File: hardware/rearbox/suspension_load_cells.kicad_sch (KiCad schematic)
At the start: 15 parts, among them U31 NAU7802SGI

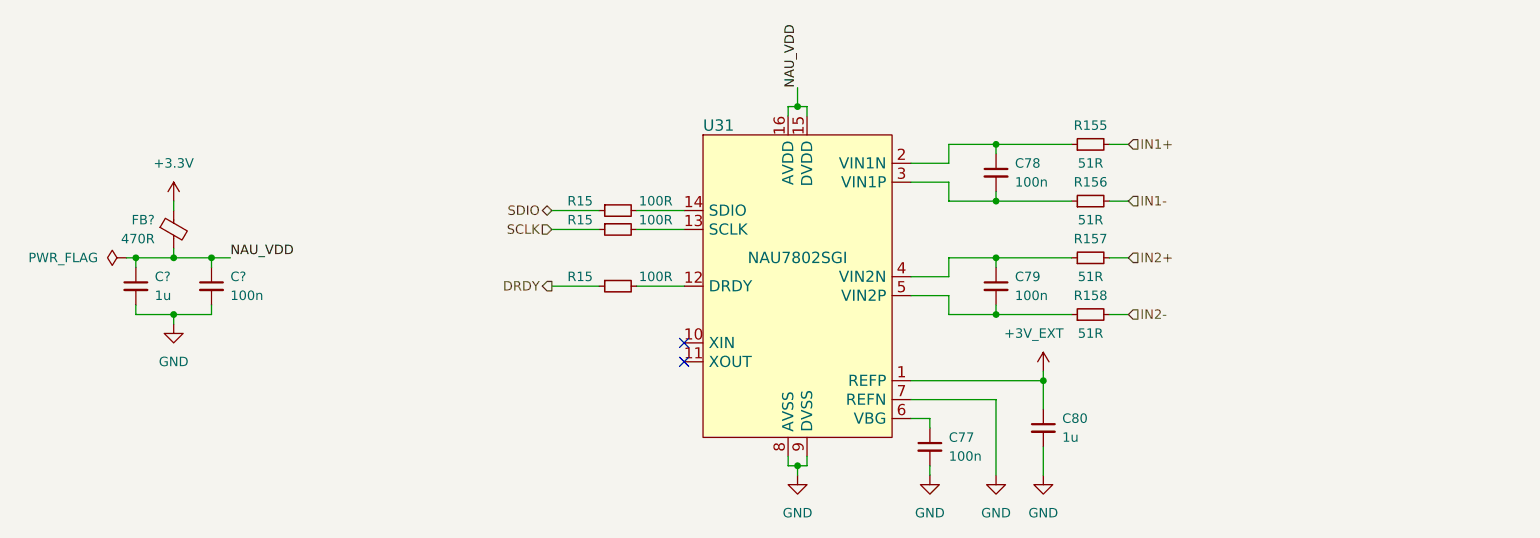
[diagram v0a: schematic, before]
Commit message: Add the connector board
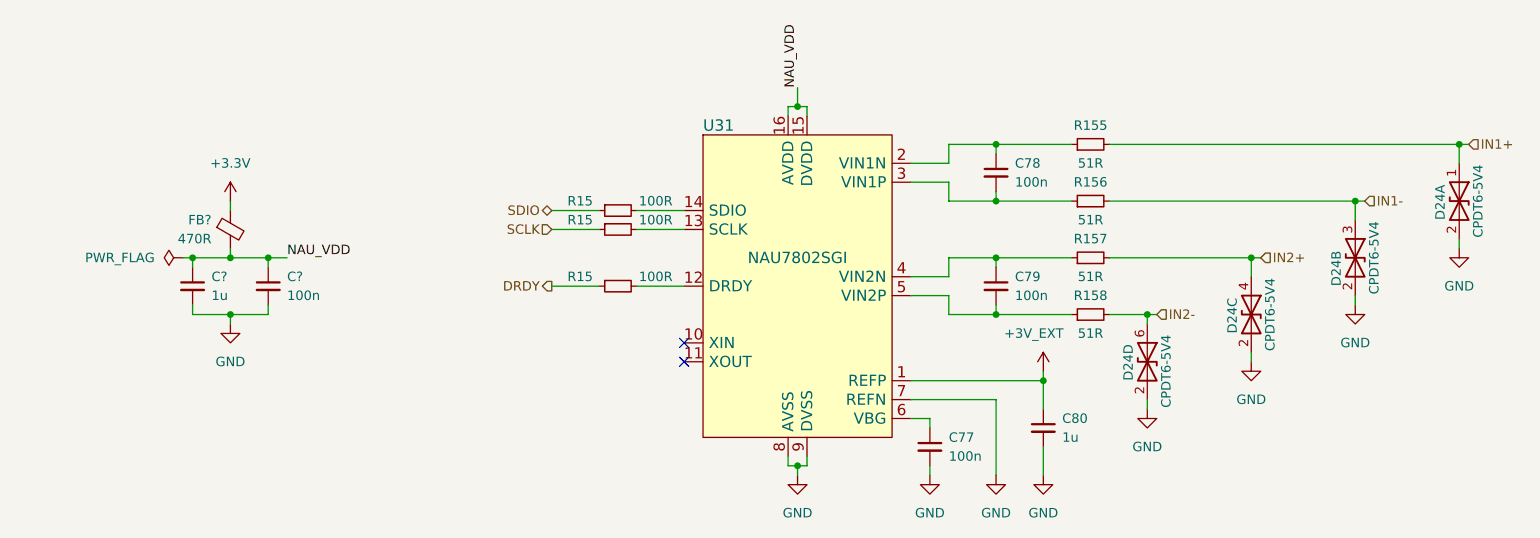
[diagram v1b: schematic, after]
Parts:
- added D24: CPDT6-5V4, Package_TO_SOT_SMD:SOT-23-6, symbol CPDT6-5V4-HF:CPDT6-5V4-HF
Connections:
- net GND: now also D24.2 (A2), D24.2 (B2), D24.2 (C2), D24.2 (D2), D24.5 (A5), D24.5 (B5), D24.5 (C5), D24.5 (D5)
- net IN1+: now also D24.1 (A1)
- net IN1-: now also D24.3 (B3)
- net IN2+: now also D24.4 (C4)
- net IN2-: now also D24.6 (D6)
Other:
- moved on the sheet: C?, FB?

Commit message: Place components on the PCB
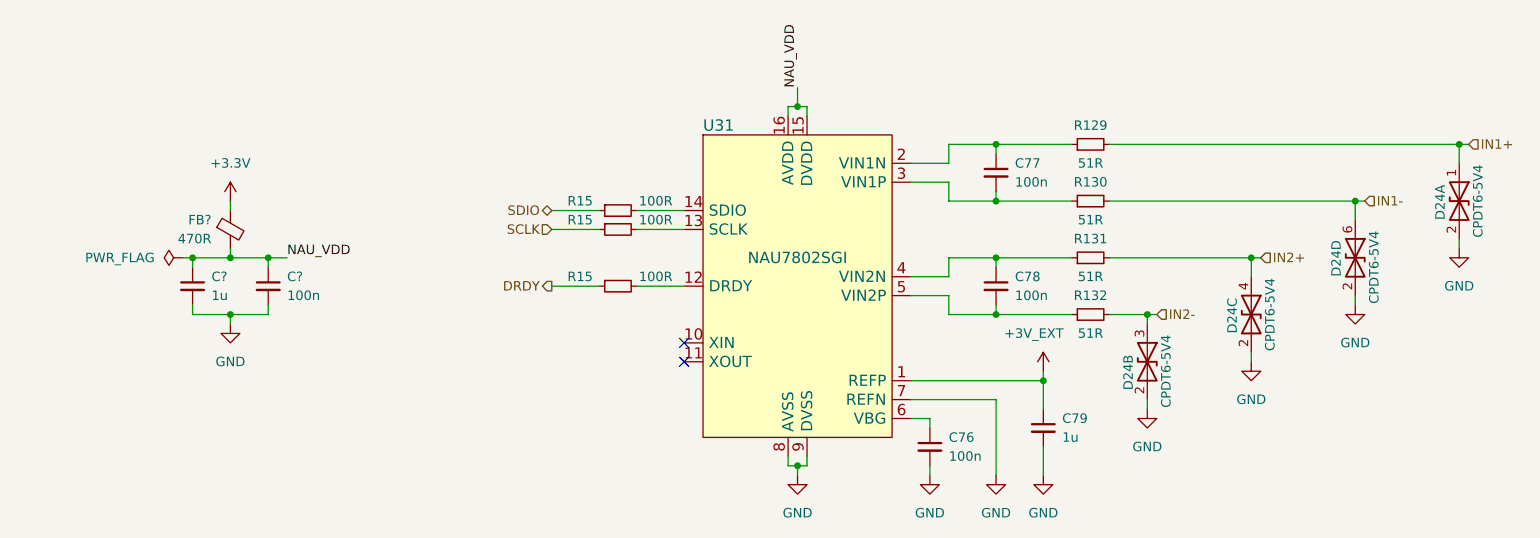
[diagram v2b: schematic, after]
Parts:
- renumbered C77 to C76, C78 to C77, C79 to C78, C80 to C79, R155 to R129, R156 to R130, R157 to R131, R158 to R132
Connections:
- net IN1-: now also D24.6 (D6); no longer D24.3 (B3)
- net IN2-: now also D24.3 (B3); no longer D24.6 (D6)
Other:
- moved on the sheet: D24B, D24D

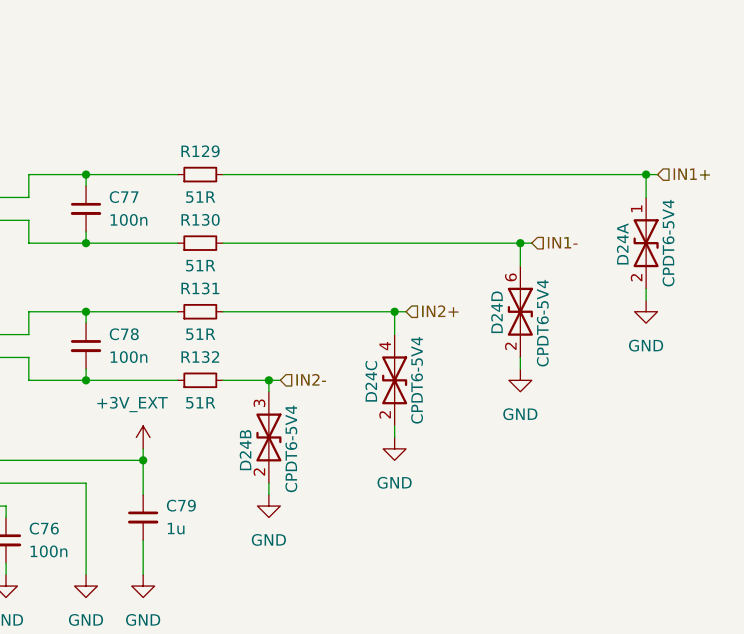
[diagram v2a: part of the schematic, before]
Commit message: Align footprint references
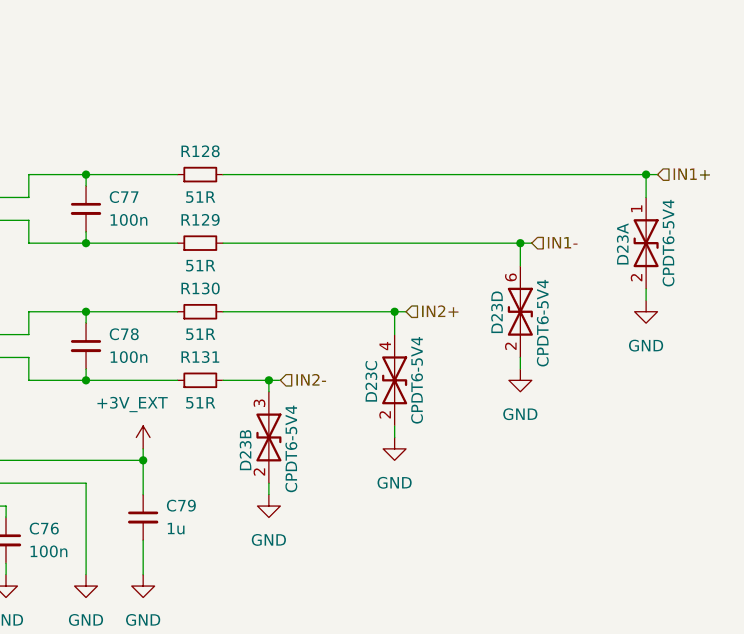
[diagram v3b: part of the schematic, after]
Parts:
- renumbered D24 to D23, R129 to R128, R130 to R129, R131 to R130, R132 to R131

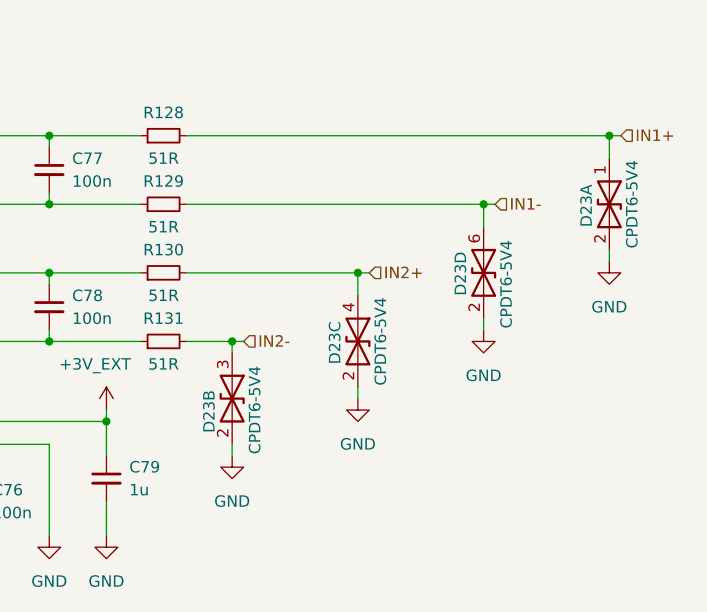
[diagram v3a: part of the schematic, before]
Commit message: Route PCB tracks
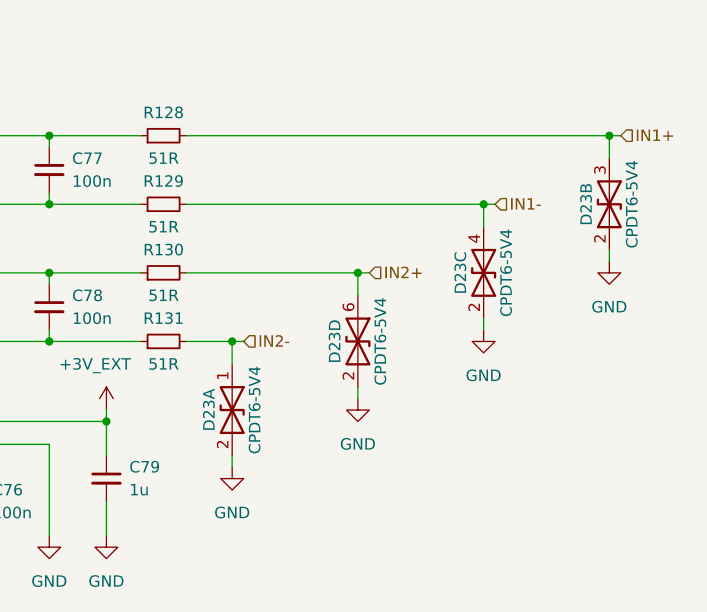
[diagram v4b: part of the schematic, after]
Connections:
- net IN1+: now also D23.3 (B3); no longer D23.1 (A1)
- net IN1-: now also D23.4 (C4); no longer D23.6 (D6)
- net IN2+: now also D23.6 (D6); no longer D23.4 (C4)
- net IN2-: now also D23.1 (A1); no longer D23.3 (B3)
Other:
- moved on the sheet: D23A, D23B, D23C, D23D
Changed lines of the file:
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@@
+    (stroke (width 0) (type default))
+  )
+  (wire (pts (xy 193.04 120.65) (xy 193.04 119.38))
     (stroke (width 0) (type default))
   )
@@
     (stroke (width 0) (type default))
   )
-  (wire (pts (xy 193.04 107.95) (xy 193.04 106.68))
+  (wire (pts (xy 193.04 109.22) (xy 193.04 106.68))
     (stroke (width 0) (type default))
   )
@@
   )
   (wire (pts (xy 179.07 114.3) (xy 179.07 115.57))
-    (stroke (width 0) (type default))
-  )
-  (wire (pts (xy 193.04 118.11) (xy 193.04 119.38))
     (stroke (width 0) (type default))
   )
@@
     )
   )
-  (symbol (lib_id "CPDT6-5V4-HF:CPDT6-5V4-HF") (at 207.01 106.68 0) (unit 3)
-    (in_bom yes) (on_board yes) (dnp no)
-    (property "Reference" "D23" (at 204.47 109.22 90)
-      (effects (font (size 1.27 1.27)) (justify left))
-    )
-    (property "Value" "CPDT6-5V4" (at 209.55 106.68 90)
-      (effects (font (size 1.27 1.27)))
-    )
-    (property "Footprint" "Package_TO_SOT_SMD:SOT-23-6" (at 207.01 120.65 0)
-      (effects (font (size 1.27 1.27)) hide)
-    )
-    (property "Datasheet" "https://www.comchiptech.com/admin/files/product/CPDT6-5V4-HF%20RevC831377.pdf" (at 207.01 123.19 0)
+  (symbol (lib_id "CPDT6-5V4-HF:CPDT6-5V4-HF") (at 220.98 99.06 0) (unit 3)
+    (in_bom yes) (on_board yes) (dnp no)
+    (property "Reference" "D23" (at 218.44 99.06 90)
+      (effects (font (size 1.27 1.27)))
+    )
+    (property "Value" "CPDT6-5V4" (at 223.52 99.06 90)
+      (effects (font (size 1.27 1.27)))
+    )
+    (property "Footprint" "Package_TO_SOT_SMD:SOT-23-6" (at 220.98 113.03 0)
+      (effects (font (size 1.27 1.27)) hide)
+    )
+    (property "Datasheet" "https://www.comchiptech.com/admin/files/product/CPDT6-5V4-HF%20RevC831377.pdf" (at 220.98 115.57 0)
       (effects (font (size 1.27 1.27)) hide)
     )
@@
     )
   )
-  (symbol (lib_id "CPDT6-5V4-HF:CPDT6-5V4-HF") (at 193.04 113.03 0) (unit 2)
-    (in_bom yes) (on_board yes) (dnp no)
-    (property "Reference" "D23" (at 190.5 116.84 90)
-      (effects (font (size 1.27 1.27)) (justify left))
-    )
-    (property "Value" "CPDT6-5V4" (at 195.58 114.3 90)
-      (effects (font (size 1.27 1.27)))
-    )
-    (property "Footprint" "Package_TO_SOT_SMD:SOT-23-6" (at 193.04 127 0)
-      (effects (font (size 1.27 1.27)) hide)
-    )
-    (property "Datasheet" "https://www.comchiptech.com/admin/files/product/CPDT6-5V4-HF%20RevC831377.pdf" (at 193.04 129.54 0)
+  (symbol (lib_id "CPDT6-5V4-HF:CPDT6-5V4-HF") (at 234.95 91.44 0) (unit 2)
+    (in_bom yes) (on_board yes) (dnp no)
+    (property "Reference" "D23" (at 232.41 91.44 90)
+      (effects (font (size 1.27 1.27)))
+    )
+    (property "Value" "CPDT6-5V4" (at 237.49 91.44 90)
+      (effects (font (size 1.27 1.27)))
+    )
+    (property "Footprint" "Package_TO_SOT_SMD:SOT-23-6" (at 234.95 105.41 0)
+      (effects (font (size 1.27 1.27)) hide)
+    )
+    (property "Datasheet" "https://www.comchiptech.com/admin/files/product/CPDT6-5V4-HF%20RevC831377.pdf" (at 234.95 107.95 0)
       (effects (font (size 1.27 1.27)) hide)
     )
@@
     )
   )
-  (symbol (lib_id "CPDT6-5V4-HF:CPDT6-5V4-HF") (at 220.98 99.06 0) (unit 4)
-    (in_bom yes) (on_board yes) (dnp no)
-    (property "Reference" "D23" (at 218.44 101.6 90)
-      (effects (font (size 1.27 1.27)) (justify left))
-    )
-    (property "Value" "CPDT6-5V4" (at 223.52 100.33 90)
-      (effects (font (size 1.27 1.27)))
-    )
-    (property "Footprint" "Package_TO_SOT_SMD:SOT-23-6" (at 220.98 113.03 0)
-      (effects (font (size 1.27 1.27)) hide)
-    )
-    (property "Datasheet" "https://www.comchiptech.com/admin/files/product/CPDT6-5V4-HF%20RevC831377.pdf" (at 220.98 115.57 0)
+  (symbol (lib_id "CPDT6-5V4-HF:CPDT6-5V4-HF") (at 207.01 106.68 0) (unit 4)
+    (in_bom yes) (on_board yes) (dnp no)
+    (property "Reference" "D23" (at 204.47 106.68 90)
+      (effects (font (size 1.27 1.27)))
+    )
+    (property "Value" "CPDT6-5V4" (at 209.55 106.68 90)
+      (effects (font (size 1.27 1.27)))
+    )
+    (property "Footprint" "Package_TO_SOT_SMD:SOT-23-6" (at 207.01 120.65 0)
+      (effects (font (size 1.27 1.27)) hide)
+    )
+    (property "Datasheet" "https://www.comchiptech.com/admin/files/product/CPDT6-5V4-HF%20RevC831377.pdf" (at 207.01 123.19 0)
       (effects (font (size 1.27 1.27)) hide)
     )
@@
     )
   )
-  (symbol (lib_id "power:GND") (at 193.04 119.38 0) (unit 1)
+  (symbol (lib_id "power:GND") (at 193.04 120.65 0) (unit 1)
     (in_bom yes) (on_board yes) (dnp no) (fields_autoplaced)
-    (property "Reference" "#PWR0250" (at 193.04 125.73 0)
-      (effects (font (size 1.27 1.27)) hide)
-    )
-    (property "Value" "GND" (at 193.04 124.46 0)
-      (effects (font (size 1.27 1.27)))
-    )
-    (property "Footprint" "" (at 193.04 119.38 0)
-      (effects (font (size 1.27 1.27)) hide)
-    )
-    (property "Datasheet" "" (at 193.04 119.38 0)
+    (property "Reference" "#PWR0250" (at 193.04 127 0)
+      (effects (font (size 1.27 1.27)) hide)
+    )
+    (property "Value" "GND" (at 193.04 125.73 0)
+      (effects (font (size 1.27 1.27)))
+    )
+    (property "Footprint" "" (at 193.04 120.65 0)
+      (effects (font (size 1.27 1.27)) hide)
+    )
+    (property "Datasheet" "" (at 193.04 120.65 0)
       (effects (font (size 1.27 1.27)) hide)
     )
@@
     )
   )
-  (symbol (lib_id "CPDT6-5V4-HF:CPDT6-5V4-HF") (at 234.95 91.44 0) (unit 1)
-    (in_bom yes) (on_board yes) (dnp no)
-    (property "Reference" "D23" (at 232.41 93.98 90)
-      (effects (font (size 1.27 1.27)) (justify left))
-    )
-    (property "Value" "CPDT6-5V4" (at 237.49 91.44 90)
-      (effects (font (size 1.27 1.27)))
-    )
-    (property "Footprint" "Package_TO_SOT_SMD:SOT-23-6" (at 234.95 105.41 0)
-      (effects (font (size 1.27 1.27)) hide)
-    )
-    (property "Datasheet" "https://www.comchiptech.com/admin/files/product/CPDT6-5V4-HF%20RevC831377.pdf" (at 234.95 107.95 0)
-      (effects (font (size 1.27 1.27)) hide)
-    )
+  (symbol (lib_id "CPDT6-5V4-HF:CPDT6-5V4-HF") (at 193.04 114.3 0) (unit 1)
+    (in_bom yes) (on_board yes) (dnp no)
+    (property "Reference" "D23" (at 190.5 114.3 90)
+      (effects (font (size 1.27 1.27)))
+    )
+    (property "Value" "CPDT6-5V4" (at 195.58 114.3 90)
+      (effects (font (size 1.27 1.27)))
+    )
+    (property "Footprint" "Package_TO_SOT_SMD:SOT-23-6" (at 193.04 128.27 0)
+      (effects (font (size 1.27 1.27)) hide)
+    )
+    (property "Datasheet" "https://www.comchiptech.com/admin/files/product/CPDT6-5V4-HF%20RevC831377.pdf" (at 193.04 130.81 0)
+      (effects (font (size 1.27 1.27)) hide)
+    )
